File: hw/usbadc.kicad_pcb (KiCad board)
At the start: 4 copper layers, 100 x 60 mm, 299 parts, among them J1 USB_C_Receptacle_USB2.0, J2 BNC, J3 BNC, J4 JTAG, J5 BNC, J7 BNC, J9 Expansion, K1 G6S-2, K2 G6S-2, Q1 SSM6N35AFE, Q2 Si3477, Q3 SSM6N35AFE, Q4 SSM6P35AFE, Q5 SSM6P35AFE, SW2 PROG, U1 TLV62569DDC, U10 CPC1017N, U11 TS5A63157DBV, U12 OPA859xDSG, U13 AD8370, U14 CPC1017N, U15 UTC2000, U16 USB3343, U18 TS5A63157DBV, U19 OPA859xDSG, U2 TLV62569DDC, U20 AD8370, U21 TCA6408A, U22 TSV992A, U23 MCP47CVB02-E_UN, U24 XC7A35T-FTG256, U25 AT25SL641, U3 TLV62569DDC, U4 SN74LVC2T45DCUR, U5 TPS563249DDC, U7 5P49V5925, U8 THS4522, U9 MAX19517, Y1 26MHz

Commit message: WIP - a lot already laid out.
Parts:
- removed C84: 100n, Capacitor_SMD:C_0603_1608Metric
- removed R63, R64: 10k, Resistor_SMD:R_0603_1608Metric
- removed R65: 5k1, Resistor_SMD:R_0603_1608Metric
- removed R66: 35k7, Resistor_SMD:R_0603_1608Metric
- removed U15: UTC2000, Package_DFN_QFN:QFN-16-1EP_3x3mm_P0.5mm_EP1.75x1.75mm_ThermalVias
- added C24: 100n, Capacitor_SMD:C_0603_1608Metric, B.Cu at (77.0, 64.7)
- added C25: 100nF, Capacitor_SMD:C_0603_1608Metric, F.Cu at (126.9, 55.3)
- added C26: 100nF, Capacitor_SMD:C_0603_1608Metric, B.Cu at (134.7, 72.5)
- added C27: 100nF, Capacitor_SMD:C_0603_1608Metric, B.Cu at (135.3, 58.6)
- added D3: LED_BARG, proj_footprints:LED_RGB_2504_horiz_barg, F.Cu at (64.4, 68.1)
- added D4: DONb, LED_SMD:LED_0603_1608Metric, F.Cu at (64.1, 65.0)
- added Q6: SSM6N35AFE, proj_footprints:SOT-563-adjusted, F.Cu at (84.0, 64.8)
- added Q7: SSM6N35AFE, proj_footprints:SOT-563-adjusted, F.Cu at (84.0, 67.3)
- added R24: 33, Resistor_SMD:R_0603_1608Metric, B.Cu at (113.3, 46.2)
- added R25: 4k7, Resistor_SMD:R_0603_1608Metric, F.Cu at (67.6, 64.2)
- added R47: 2k, Resistor_SMD:R_0603_1608Metric, F.Cu at (67.6, 65.7)
- added R51: 230, Resistor_SMD:R_0603_1608Metric, F.Cu at (70.5, 68.9)
- added TP1: GND, usbadc_local:single_pad, F.Cu at (111.6, 57.6)
- C102, C147, C40, C56, C67, C69, C70, C79, C81, C82, C96, R61, R71, R80, R82, R86, R88, R90, R91, U10, U14: moved to B.Cu
- C105, C22, C94, C95, C98: footprint Capacitor_SMD:C_0402_1005Metric -> Capacitor_SMD:C_0603_1608Metric; moved to B.Cu
- C23: value 100n -> 100nF; footprint Capacitor_SMD:C_0402_1005Metric -> Capacitor_SMD:C_0603_1608Metric
- C68, C77, C80, C9: footprint Capacitor_SMD:C_0402_1005Metric -> Capacitor_SMD:C_0603_1608Metric
- J1: footprint proj_footprints:USB_C_Receptacle_GCT_USB4085_smaller_holes -> proj_footprints:USB_C_Receptacle_Molex_2171790001_16P_TopMnt_Horizontal
- JP1: value PUDC_dis -> PUDC
- R12: value 10k -> 0
- R26: value 10k -> 750
- R30, R31, R32, R33: footprint Resistor_SMD:R_0603_1608Metric -> Resistor_SMD:R_0402_1005Metric
- moved R98 161.8 mm to (137.0, 58.6), turned to 90 degrees
- moved R52 155.1 mm to (151.8, 58.6)
- moved R108 147.1 mm to (105.2, 67.4), turned to -90 degrees
- moved R99 146.9 mm to (124.6, 72.3)
- moved R97 145.2 mm to (124.6, 75.3)
- moved R96 145.1 mm to (124.6, 73.8)
- moved C78 143.7 mm to (148.0, 53.0)
- moved C82 140.8 mm to (137.9, 50.8), turned to 90 degrees
- moved JP3 140.6 mm to (108.6, 78.0), turned to 90 degrees
- moved C79 136.7 mm to (140.9, 56.0)
- moved Q5 133.1 mm to (116.0, 77.0), turned to 90 degrees
- moved C81 133.1 mm to (137.2, 58.3), turned to -90 degrees
- moved Q4 133.0 mm to (116.0, 74.8), turned to 90 degrees
- moved D8 131.7 mm to (141.0, 39.4), turned to 180 degrees
- moved R107 131.4 mm to (91.3, 73.3), turned to 180 degrees
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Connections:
- net Net-(U20-INLO) renamed /Front End/FE_CHB/PGA_INLO
- C111 pad 2: /Front End/FE_CHA/PGA_INHI -> /Front End/FE_CHA/PGA_INLO
- C113 pad 1: /Front End/FE_CHA/PGA_INHI -> /Front End/FE_CHA/PGA_INLO
- C23 pad 1: +1V8 -> +2V5_analog
- C23 pad 2: GND -> -2V5_analog
- C63 pad 2: Net-(U7-OUT4) -> Net-(U7-OUT3)
- C70 pad 2: +5V -> Vpp_analog
- C82 pad 2: +5V -> Vpp_analog
- C83 pad 2: Net-(U7-OUT4B) -> Net-(U7-OUT3B)
- FB1 pad 1: Net-(FB1-Pad1) -> +5V_switched
- K1 pad 4: Net-(JP4-C) -> GND
- K1 pad 5: GND -> Net-(JP4-C)
- K2 pad 4: Net-(JP5-C) -> GND
- K2 pad 5: GND -> Net-(JP5-C)
- Q1 pad 2: IO_L23N_T3_35 -> /Front End/fe_ctl/P0
- Q1 pad 5: IO_L23N_T3_35 -> /Front End/fe_ctl/P0
- Q2 pad 1: Net-(FB1-Pad1) -> +5V_switched
- Q2 pad 2: Net-(FB1-Pad1) -> +5V_switched
- Q2 pad 5: Net-(FB1-Pad1) -> +5V_switched
- Q2 pad 6: Net-(FB1-Pad1) -> +5V_switched
- Q3 pad 2: IO_L23P_T3_35 -> /Front End/fe_ctl/P1
- Q3 pad 5: IO_L23P_T3_35 -> /Front End/fe_ctl/P1
- Q4 pad 2: IO_L21P_T3_DQS_35 -> IO_L8P_T1_D11_14
- Q4 pad 3: /Front End/FE_CHA/PGA_CTL_DATA -> /Front End/FE_CHA/PGA_CTL_CLK
- Q4 pad 5: /Front End/PGA_SDAT -> IO_L8N_T1_D12_14
- Q4 pad 6: /Front End/FE_CHA/PGA_CTL_CLK -> /Front End/FE_CHA/PGA_CTL_LATCH
- Q5 pad 2: IO_L22N_T3_35 -> IO_L9N_T1_DQS_D13_14
- Q5 pad 3: /Front End/FE_CHA/PGA_CTL_LATCH -> /Front End/FE_CHB/PGA_CTL_LATCH
- Q5 pad 5: IO_L22P_T3_35 -> IO_L12N_T1_MRCC_14
- Q5 pad 6: /Front End/FE_CHB/PGA_CTL_LATCH -> /Front End/FE_CHA/PGA_CTL_DATA
- R12 pad 1: Net-(J1-CC2) -> IO_L22N_T3_35
- R12 pad 2: Net-(U15-CC2) -> Net-(U16-~{RESETB})
- R16 pad 2: /USB/ULPI_RSTb -> Net-(U16-~{RESETB})
- R19 pad 1: IO_L9N_T1_DQS_34 -> IO_L7N_T1_34
- R21 pad 1: IO_L10P_T1_34 -> IO_L8N_T1_34
- R26 pad 1: Net-(J1-CC1) -> Net-(D3-RK)
- R27 pad 2: Net-(U7-OUT3) -> Net-(U7-OUT2)
- R93 pad 1: /Front End/FE_CHA/PGA_INHI -> /Front End/FE_CHA/PGA_INLO
- R95 pad 1: /Front End/FE_CHA/PGA_INHI -> /Front End/FE_CHA/PGA_INLO
- U10 pad 3: Net-(J2-In) -> Net-(JP4-B)
- U10 pad 4: Net-(JP4-B) -> Net-(J2-In)
- U11 pad 5: +5V -> Vpp_analog
- U12 pad 6: Net-(U13-INLO) -> /Front End/FE_CHA/PGA_INHI
- U13 pad 16: Net-(U13-INLO) -> /Front End/FE_CHA/PGA_INLO
- U13 pad 8: /ADC+Driver/ADC_CHA_IN_N -> /ADC+Driver/ADC_CHA_IN_P
- U13 pad 9: /ADC+Driver/ADC_CHA_IN_P -> /ADC+Driver/ADC_CHA_IN_N
- U14 pad 3: Net-(J3-In) -> Net-(JP5-B)
- U14 pad 4: Net-(JP5-B) -> Net-(J3-In)
- U16 pad 22: /USB/ULPI_RSTb -> Net-(U16-~{RESETB})
- U18 pad 5: +5V -> Vpp_analog
- U20 pad 8: /ADC+Driver/ADC_CHB_IN_N -> /ADC+Driver/ADC_CHB_IN_P
- U20 pad 9: /ADC+Driver/ADC_CHB_IN_P -> /ADC+Driver/ADC_CHB_IN_N
- U21 pad 10: /Front End/fe_ctl/P7 -> /Front End/FE_CHA/FE_CTL_AC
- U21 pad 14: Vpp_analog -> +5V_switched
- U21 pad 3: /Front End/FE_CHB/FE_CTL_TERM -> /Front End/fe_ctl/P1
- U21 pad 4: /Front End/FE_CHB/FE_CTL_AC -> /Front End/FE_CHB/FE_CTL_ATT
- U21 pad 5: /Front End/FE_CHB/FE_CTL_ATT -> /Front End/FE_CHB/FE_CTL_AC
- U21 pad 7: /Front End/FE_CHA/FE_CTL_ATT -> /Front End/FE_CHB/FE_CTL_TERM
- U21 pad 8: /Front End/FE_CHA/FE_CTL_AC -> /Front End/FE_CHA/FE_CTL_TERM
- U21 pad 9: /Front End/FE_CHA/FE_CTL_TERM -> /Front End/FE_CHA/FE_CTL_ATT
- U4 pad 5: IO_L10P_T1_34 -> IO_L8N_T1_34
- U7 pad 11: Net-(U7-OUT4) -> unconnected-(U7-OUT4-Pad11)
- U7 pad 12: Net-(U7-OUT4B) -> unconnected-(U7-OUT4B-Pad12)
- U7 pad 13: unconnected-(U7-OUT3B-Pad13) -> Net-(U7-OUT3B)
- U7 pad 17: unconnected-(U7-OUT2-Pad17) -> Net-(U7-OUT2)
- U7 pad 20: IO_L12N_T1_MRCC_15 -> Net-(U7-OUT1)
- U9 pad 45: IO_L18P_T2_35 -> IO_L7P_T1_D09_14
- U9 pad 46: IO_L17N_T2_35 -> IO_L3N_T0_DQS_EMCCLK_14
- U9 pad 47: IO_L18N_T2_35 -> IO_L7N_T1_D10_14
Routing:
- net GND: track 100.4 -> 282.1 mm, vias 44 -> 154
- net -2V5_analog: track 0.00 -> 75.1 mm, vias 0 -> 15
- net /Front End/FE_CHA/FE_CTL_TERM: track 0.00 -> 71.5 mm
- net /Front End/FE_CHA/FE_CTL_ATT: track 0.00 -> 66.1 mm
- net /Front End/FE_CHA/FE_CTL_AC: track 0.00 -> 61.9 mm
- net /Front End/FE_CHA/PGA_CTL_DATA: track 0.00 -> 53.8 mm, vias 0 -> 4
- net Vpp_analog: track 0.00 -> 53.6 mm, vias 0 -> 5
- net +2V5_analog: track 0.00 -> 51.7 mm, vias 0 -> 13
- net /Front End/FE_CHA/PGA_CTL_CLK: track 0.00 -> 48.8 mm, vias 0 -> 4
- net /Front End/FE_CHB/FE_CTL_AC: track 0.00 -> 45.4 mm
- net /Front End/FE_CHB/PGA_CTL_LATCH: track 0.00 -> 42.5 mm, vias 0 -> 4
- net /Front End/FE_CHA/PGA_INLO: track 0.00 -> 35.4 mm, vias 0 -> 2
- net /FPGA A7/DONE: track 6.24 -> 39.7 mm, vias 0 -> 2
- net +1V8: track 88.1 -> 115.9 mm, vias 29 -> 38
- net +1V8_analog: track 0.00 -> 25.6 mm, vias 0 -> 4
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- added copper zone on In2.Cu, net +2V5_analog
- added copper zone on In2.Cu, net -2V5_analog
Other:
- board text added: "1V8 GND TCK TDO TDI TMS"

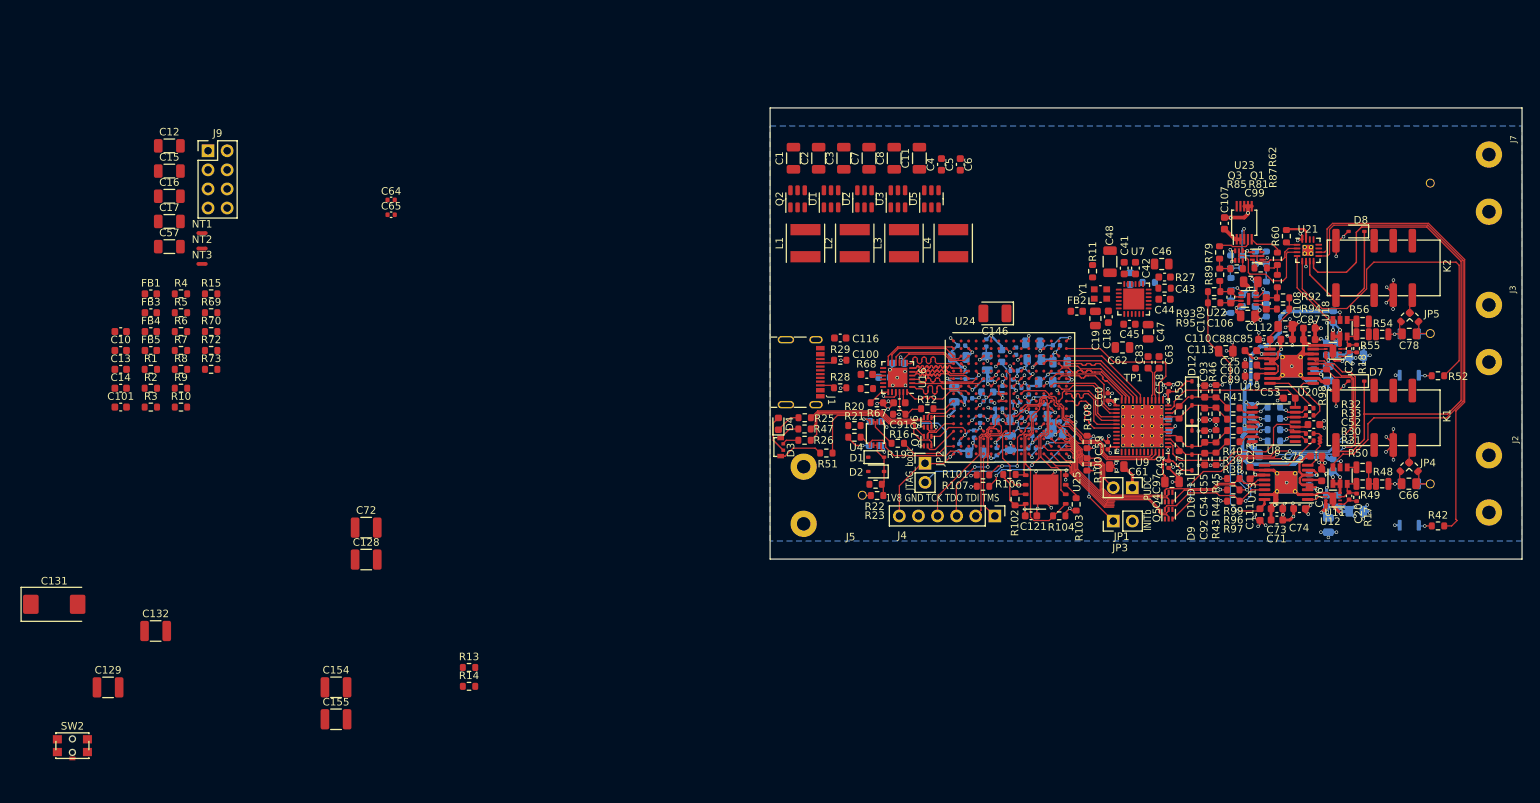
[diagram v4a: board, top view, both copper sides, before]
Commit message: WIP - almost everything except power (converters) connected
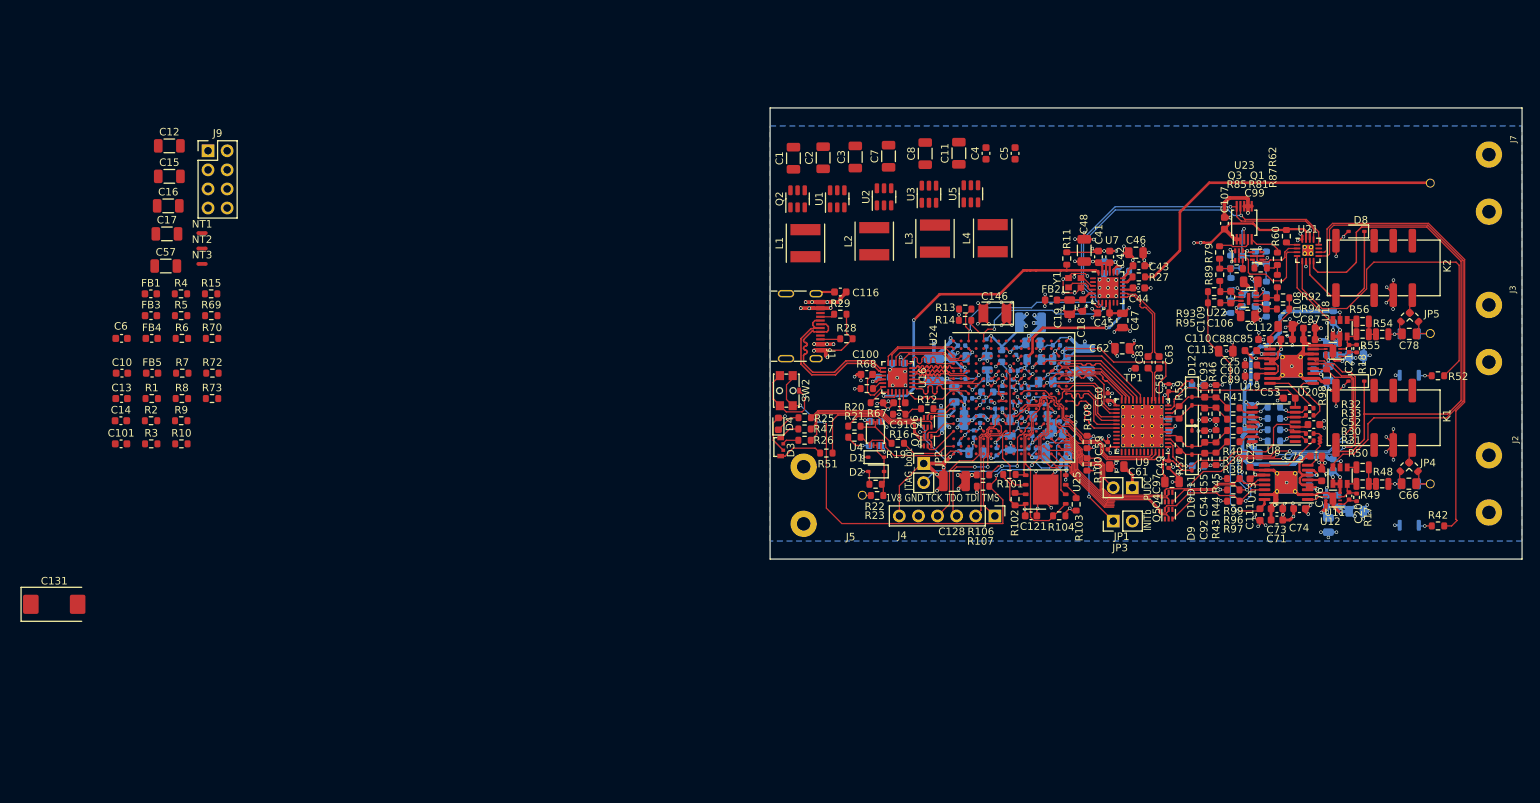
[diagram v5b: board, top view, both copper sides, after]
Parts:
- C129, C132, C154, C155, C72: moved to B.Cu
- C64, C65: footprint Capacitor_SMD:C_0402_1005Metric -> Capacitor_SMD:C_0603_1608Metric; moved to B.Cu
- moved C129 131.9 mm to (97.6, 51.5)
- moved C64 113.0 mm to (119.9, 70.6), turned to 180 degrees
- moved C132 109.7 mm to (87.3, 64.5), turned to 180 degrees
- moved C65 109.6 mm to (119.9, 59.9)
- moved SW2 106.0 mm to (65.2, 60.6), turned to 90 degrees
- moved C154 100.8 mm to (101.2, 69.0)
- moved C72 98.2 mm to (104.8, 56.5), turned to -90 degrees
- moved C155 92.1 mm to (84.8, 57.8), turned to 90 degrees
- moved R14 82.0 mm to (88.9, 51.2), turned to 180 degrees
- moved R13 81.4 mm to (89.0, 49.8), turned to 180 degrees
- moved C128 78.9 mm to (87.5, 72.6)
- moved C5 7.43 mm to (95.6, 29.0)
- moved R28 6.58 mm to (73.2, 53.7)
- moved C116 6.12 mm to (72.3, 47.5)
- moved J1 6.12 mm to (66.0, 52.0)
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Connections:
- net Net-(U7-OUT3) renamed /Clock/PLL_O3_P
- net Net-(U7-OUT3B) renamed /Clock/PLL_O3_N
- R13 pad 1: IO_L20N_T3_35 -> IO_L4N_T0_35
- R14 pad 1: IO_L20P_T3_35 -> IO_L3P_T0_DQS_AD5P_35
- R24 pad 1: IO_L12N_T1_MRCC_15 -> IO_L11P_T1_SRCC_15
- U21 pad 12: IO_L20P_T3_35 -> IO_L3P_T0_DQS_AD5P_35
- U21 pad 13: IO_L20N_T3_35 -> IO_L4N_T0_35
- U23 pad 10: IO_L20N_T3_35 -> IO_L4N_T0_35
- U23 pad 9: IO_L20P_T3_35 -> IO_L3P_T0_DQS_AD5P_35
- U7 pad 8: IO_L20N_T3_35 -> IO_L4N_T0_35
- U7 pad 9: IO_L20P_T3_35 -> IO_L3P_T0_DQS_AD5P_35
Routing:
- net GND: track 282.1 -> 409.4 mm, vias 154 -> 215
- net +1V8: track 115.9 -> 199.4 mm, vias 38 -> 62
- net IO_L4N_T0_35: track 0.00 -> 70.8 mm, vias 0 -> 3
- net IO_L3P_T0_DQS_AD5P_35: track 0.00 -> 70.2 mm, vias 0 -> 3
- net Net-(U24C-PROGRAM_B_0): track 22.8 -> 74.3 mm, vias 2 -> 4
- net /Clock/CLK_OUT: track 0.00 -> 46.1 mm
- net /Clock/USB_REF_CLK: track 2.24 -> 44.0 mm, vias 1 -> 2
- net IO_L11P_T1_SRCC_15: track 0.00 -> 22.0 mm, vias 0 -> 1
- net /USB/USBin_N: track 0.00 -> 21.7 mm
- net /USB/USBin_P: track 0.00 -> 21.6 mm
- net +1V8_analog: track 25.6 -> 40.2 mm, vias 4 -> 7
- net +5V: track 7.43 -> 20.4 mm, vias 1 -> 11
- net /Clock/PLL_O3_P: track 0.00 -> 11.3 mm
- net /Clock/PLL_O3_N: track 0.00 -> 11.3 mm
- net +1V0: track 22.1 -> 29.3 mm, vias 9 -> 13
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- added copper zone on In2.Cu, net +1V8_analog
- added copper zone on In2.Cu, net +5V

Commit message: layout finished (draft)
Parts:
- removed C101: 100n, Capacitor_SMD:C_0603_1608Metric
- removed NT1, NT2, NT3: Net-Tie_2, NetTie:NetTie-2_SMD_Pad0.5mm
- removed R70: 0, Resistor_SMD:R_0603_1608Metric
- added C28: 10u, Capacitor_SMD:C_1206_3216Metric, B.Cu at (119.3, 54.1)
- added D5: LED_BARG, proj_footprints:LED_RGB_2504_horiz_barg, F.Cu at (162.0, 65.0)
- added D6: LED_BARG, proj_footprints:LED_RGB_2504_horiz_barg, F.Cu at (162.0, 45.0)
- added Q10: SSM6N35AFE, proj_footprints:SOT-563-adjusted, F.Cu at (157.6, 44.1)
- added Q8: DMC2053UVT, Package_TO_SOT_SMD:TSOT-23-6, F.Cu at (107.2, 36.5)
- added Q9: SSM6N35AFE, proj_footprints:SOT-563-adjusted, F.Cu at (157.7, 63.6)
- added R53: 2k, Resistor_SMD:R_0603_1608Metric, F.Cu at (160.1, 66.8)
- added R58: 230, Resistor_SMD:R_0603_1608Metric, F.Cu at (160.1, 63.8)
- added R63: 750, Resistor_SMD:R_0603_1608Metric, F.Cu at (160.1, 65.3)
- added R64: 750, Resistor_SMD:R_0603_1608Metric, F.Cu at (160.0, 45.3)
- added R65: 2k, Resistor_SMD:R_0603_1608Metric, F.Cu at (160.0, 46.8)
- added R66: 230, Resistor_SMD:R_0603_1608Metric, F.Cu at (160.0, 43.8)
- C13, FB1, R42: moved to B.Cu
- C17: value 10u -> 100n; footprint Capacitor_SMD:C_1206_3216Metric -> Capacitor_SMD:C_0603_1608Metric; moved to B.Cu
- L1, L2, L3, L4: value 2u2 -> 1u5; footprint Inductor_SMD:L_Taiyo-Yuden_NR-50xx -> Inductor_SMD:L_1008_2520Metric
- Q2: value Si3477 -> SSM6N35AFE; footprint Package_TO_SOT_SMD:TSOT-23-6 -> proj_footprints:SOT-563-adjusted
- U1, U2, U3: value TLV62569DDC -> RT8096B
- moved FB1 140.8 mm to (121.4, 43.4), turned to -90 degrees
- moved C131 140.1 mm to (97.8, 36.9)
- moved C17 135.3 mm to (117.3, 54.2), turned to 90 degrees
- moved FB4 133.2 mm to (113.2, 38.8)
- moved FB3 121.2 mm to (100.1, 29.8)
- moved R3 118.9 mm to (94.3, 32.4)
- moved R73 118.2 mm to (104.5, 37.2), turned to -90 degrees
- moved R7 110.2 mm to (92.1, 33.2), turned to 90 degrees
- moved C6 109.2 mm to (85.4, 42.8), turned to 90 degrees
- moved C16 108.2 mm to (91.0, 40.1), turned to 180 degrees
- moved R72 107.6 mm to (94.8, 40.1)
- moved C14 106.0 mm to (78.2, 34.2), turned to 180 degrees
- moved R1 105.5 mm to (83.9, 39.4), turned to -90 degrees
- moved FB5 105.0 mm to (82.2, 31.2)
- moved R4 104.6 mm to (89.1, 42.0)
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- renumbered U21 to locked
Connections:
- net /Power/PG_2V5 renamed /Power/5V_EN
- C17 pad 1: Net-(C16-Pad1) -> GND
- C17 pad 2: GND -> +1V8_analog
- FB3 pad 1: +2V5 -> Net-(C5-Pad1)
- J9 pad 2: -2V5_analog -> +2V5_analog
- J9 pad 3: IO_L19P_T3_35 -> IO_L3P_T0_DQS_AD5P_35
- J9 pad 4: +1V8 -> -2V5_analog
- J9 pad 5: IO_L19N_T3_VREF_35 -> IO_L3N_T0_DQS_AD5N_35
- J9 pad 6: +2V5 -> +1V8
- Q2 pad 1: +5V_switched -> GND
- Q2 pad 2: +5V_switched -> IO_L16N_T2_A15_D31_14
- Q2 pad 3: Net-(Q2-G) -> Net-(Q2B-D)
- Q2 pad 4: +5V -> GND
- Q2 pad 5: +5V_switched -> IO_L23N_T3_A02_D18_14
- Q2 pad 6: +5V_switched -> Net-(Q2A-D)
- R13 pad 1: IO_L4N_T0_35 -> IO_L2N_T0_AD12N_35
- R14 pad 1: IO_L3P_T0_DQS_AD5P_35 -> IO_L2P_T0_AD12P_35
- R2 pad 2: Net-(NT1-Pad1) -> GND
- R3 pad 2: Net-(NT2-Pad1) -> GND
- R4 pad 2: Net-(NT3-Pad1) -> GND
- R73 pad 1: Net-(Q2-G) -> +5V
- R73 pad 2: /Power/PWR_EN -> Net-(Q8A-D)
- U23 pad 10: IO_L4N_T0_35 -> IO_L2N_T0_AD12N_35
- U23 pad 9: IO_L3P_T0_DQS_AD5P_35 -> IO_L2P_T0_AD12P_35
- U7 pad 8: IO_L4N_T0_35 -> IO_L2N_T0_AD12N_35
- U7 pad 9: IO_L3P_T0_DQS_AD5P_35 -> IO_L2P_T0_AD12P_35
- locked pad 12: IO_L3P_T0_DQS_AD5P_35 -> IO_L2P_T0_AD12P_35
- locked pad 13: IO_L4N_T0_35 -> IO_L2N_T0_AD12N_35
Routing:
- net GND: track 409.4 -> 509.7 mm, vias 215 -> 266
- net IO_L23N_T3_A02_D18_14: track 0.00 -> 89.7 mm
- net IO_L9P_T1_DQS_14: track 11.7 -> 96.6 mm
- net IO_L16P_T2_CSI_B_14: track 13.7 -> 97.4 mm
- net IO_L2N_T0_AD12N_35: track 0.00 -> 73.9 mm, vias 0 -> 3
- net IO_L2P_T0_AD12P_35: track 0.00 -> 71.7 mm, vias 0 -> 3
- net +2V5_analog: track 51.7 -> 123.3 mm, vias 13 -> 34
- net IO_L4N_T0_35: track 70.8 -> 0.00 mm, vias 3 -> 0
- net IO_L10N_T1_D15_14: track 10.8 -> 77.1 mm
- net IO_L10P_T1_D14_14: track 11.8 -> 78.0 mm
- net IO_L16N_T2_A15_D31_14: track 12.7 -> 76.7 mm
- net +5V: track 20.4 -> 73.5 mm, vias 11 -> 37
- net +1V8: track 199.4 -> 245.6 mm, vias 62 -> 75
- net IO_L3N_T0_DQS_AD5N_35: track 0.00 -> 36.9 mm, vias 0 -> 1
- net +5V_switched: track 1.22 -> 36.8 mm, vias 1 -> 6
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- added copper zone on B.Cu, net +2V5_analog
- added copper zone on F.Cu, net GND
